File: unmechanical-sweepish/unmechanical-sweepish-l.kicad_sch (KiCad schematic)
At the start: 82 parts, among them J6 M, Q2 AO3400A, U10 74HC4051, U4 OPA340NA

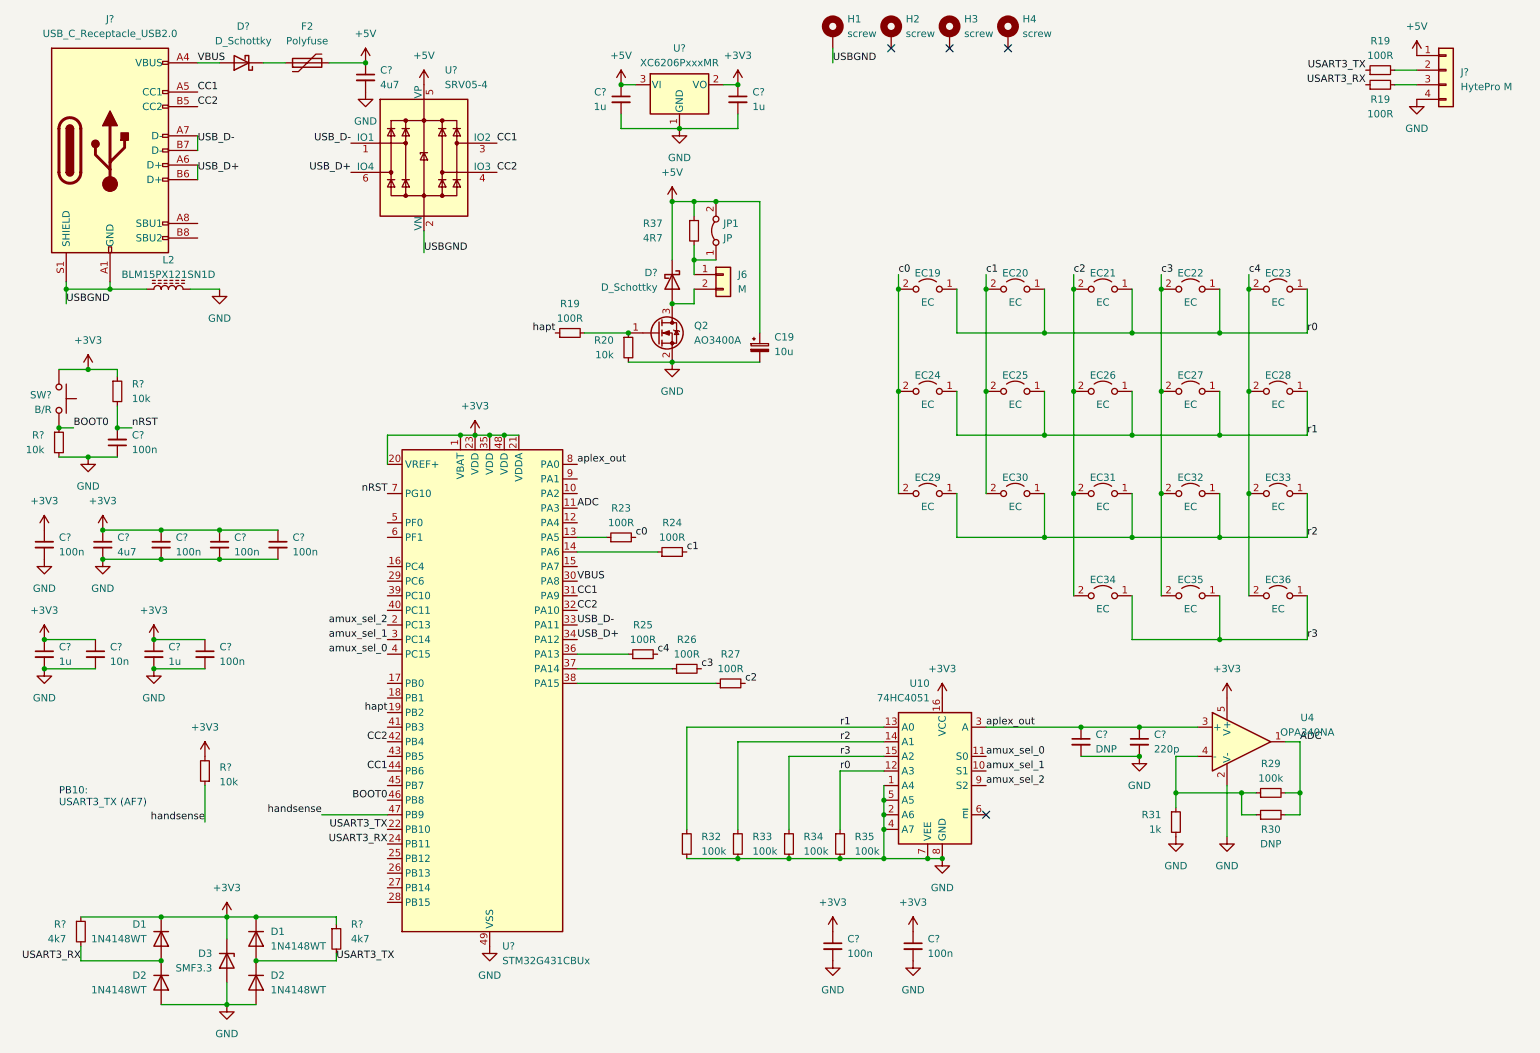
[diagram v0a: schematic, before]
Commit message: Migrate to v8
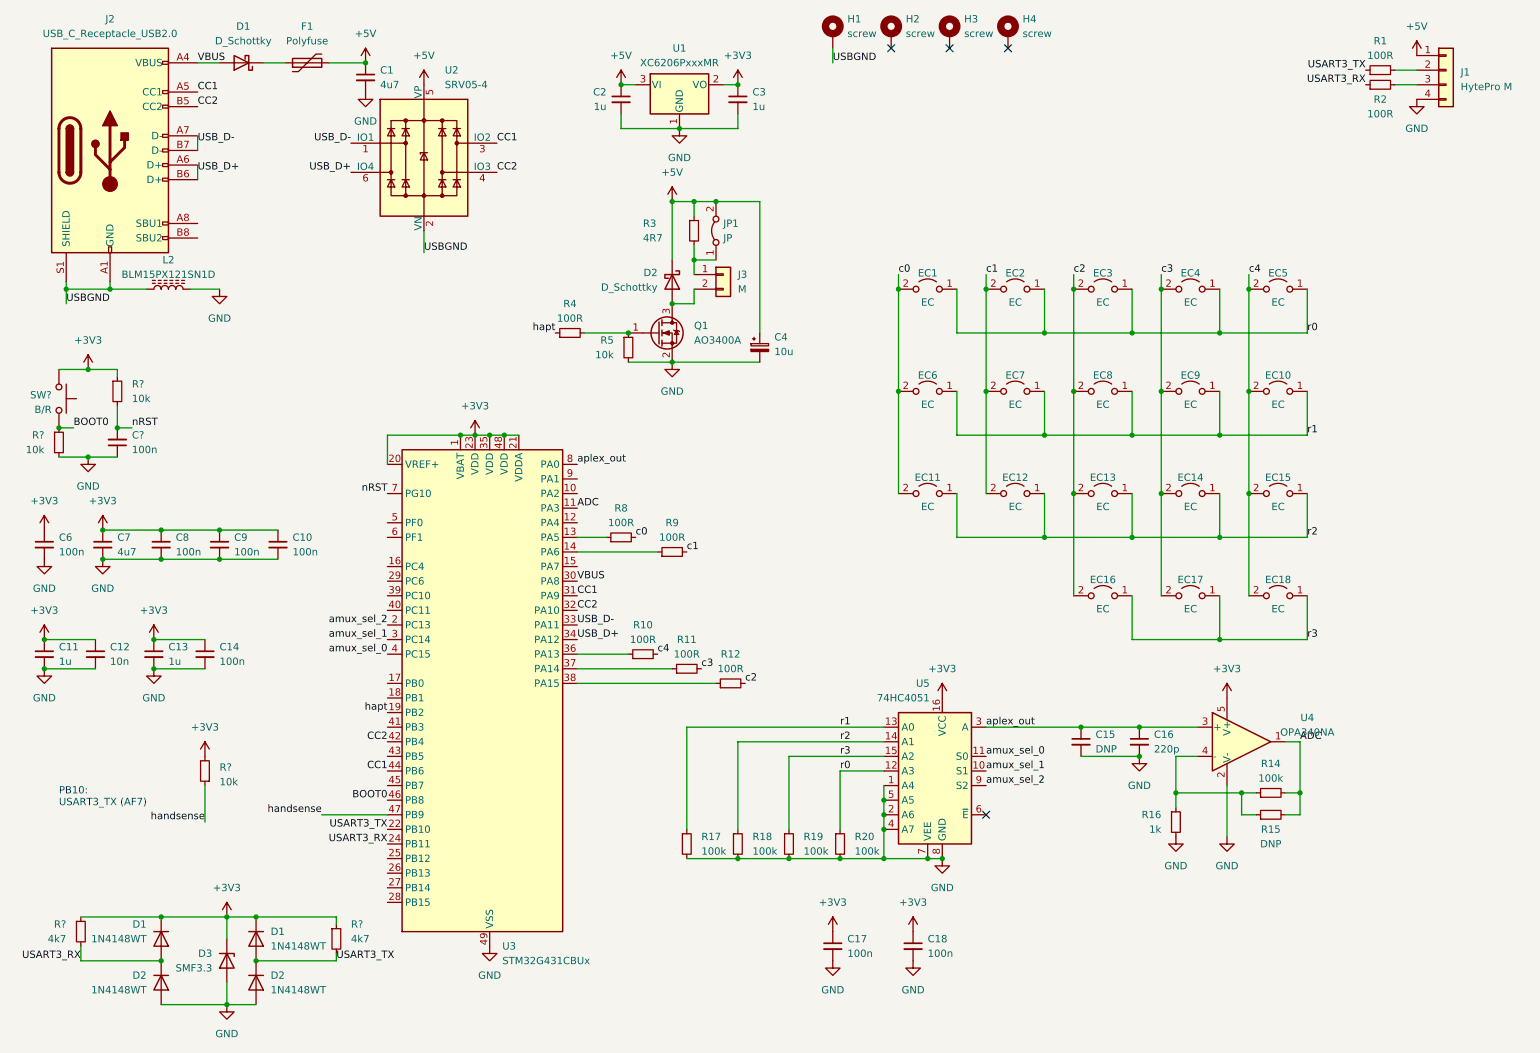
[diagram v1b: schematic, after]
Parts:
- L2: value BLM15PX121SN1D -> BLM15PX121SN1D
- gave numbers to parts that had none: 23
- renumbered C19 to C4, EC19 to EC1, EC28 to EC10, EC29 to EC11, EC30 to EC12, EC31 to EC13, EC32 to EC14, EC33 to EC15, EC34 to EC16, EC35 to EC17, EC36 to EC18, EC20 to EC2, EC21 to EC3, EC22 to EC4, EC23 to EC5, EC24 to EC6, EC25 to EC7, EC26 to EC8, EC27 to EC9, F2 to F1, J6 to J3, Q2 to Q1, R19 to R1, R25 to R10, R26 to R11, R27 to R12, R29 to R14, R30 to R15, R31 to R16, R32 to R17, R33 to R18, R34 to R19, R19 to R2, R35 to R20, R37 to R3, R19 to R4, R20 to R5, R23 to R8, R24 to R9, U10 to U5

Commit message: Fix up for order
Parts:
- J1: footprint PCM_marbastlib-xp-various:CON_HytePro_M411P_Plug_1x04-P2.20mm_Horizontal_FlushMount -> Connector_PinHeader_2.54mm:PinHeader_1x04_P2.54mm_Vertical
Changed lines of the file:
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@@
 			)
 		)
-		(property "Footprint" "PCM_marbastlib-xp-various:CON_HytePro_M411P_Plug_1x04-P2.20mm_Horizontal_FlushMount"
+		(property "Footprint" "Connector_PinHeader_2.54mm:PinHeader_1x04_P2.54mm_Vertical"
 			(at 261.62 25.4 0)
 			(effects
